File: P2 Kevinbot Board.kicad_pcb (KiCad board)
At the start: 4 copper layers, 156.5 x 85.4 mm, 45 parts, among them J1 Conn_01x03_Pin, J12 Conn_02x06_Odd_Even, J16 Conn_02x06_Odd_Even, J2 Conn_01x03_Pin, J3 USB_C_Receptacle_USB2.0_16P, J4 Conn_01x02_Pin, J5 Conn_01x02_Pin, J6 Conn_02x06_Odd_Even, J7 Conn_01x02_Pin, J8 Conn_02x06_Odd_Even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

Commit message: reset button
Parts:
- added J9: Conn_01x02_Pin, Connector_Molex:Molex_Nano-Fit_105309-xx02_1x02_P2.50mm_Vertical, F.Cu at (125.3, 58.9)
- added SW1: SW_Push, Button_Switch_SMD:SW_SPST_PTS645, F.Cu at (129.0, 96.4)
- moved JP1 4.20 mm to (120.2, 70.1)
- moved JP3 4.20 mm to (120.2, 72.7)
- moved JP2 4.20 mm to (120.2, 67.5)
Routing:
- net /P2_RESn: track 44.1 -> 88.9 mm, vias 1 -> 3
- net /Programmer/TX: track 14.2 -> 18.0 mm
- net P2_P63_RXD: track 46.2 -> 42.5 mm
- net P2_P62_TXD: track 51.2 -> 47.9 mm
- net /Programmer/RX: track 16.7 -> 19.8 mm
- net /Programmer/RESn: track 7.93 -> 9.67 mm
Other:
- board text added: "CORE RESET"

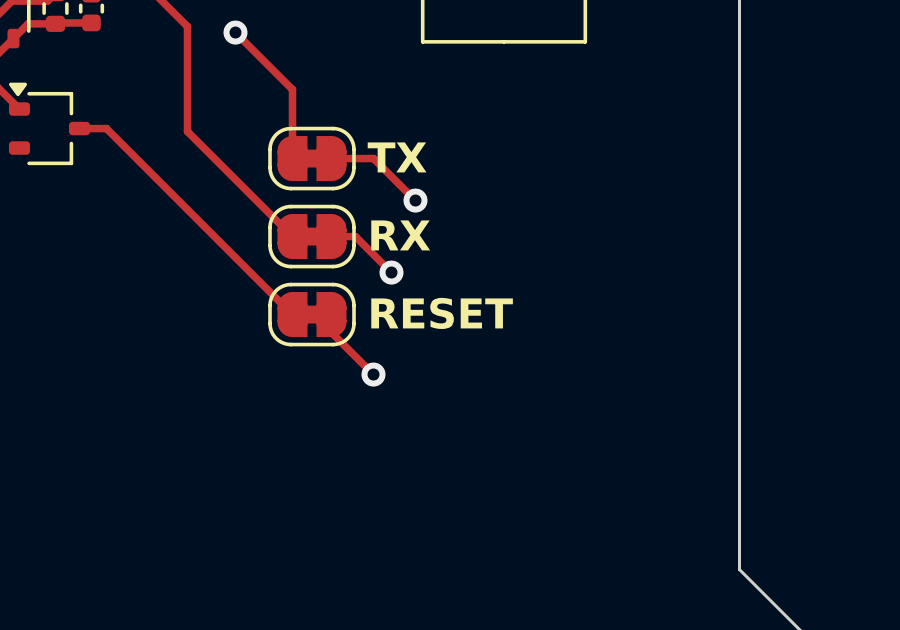
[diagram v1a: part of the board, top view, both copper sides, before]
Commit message: docs: add logo banner, pcb: reset text changes
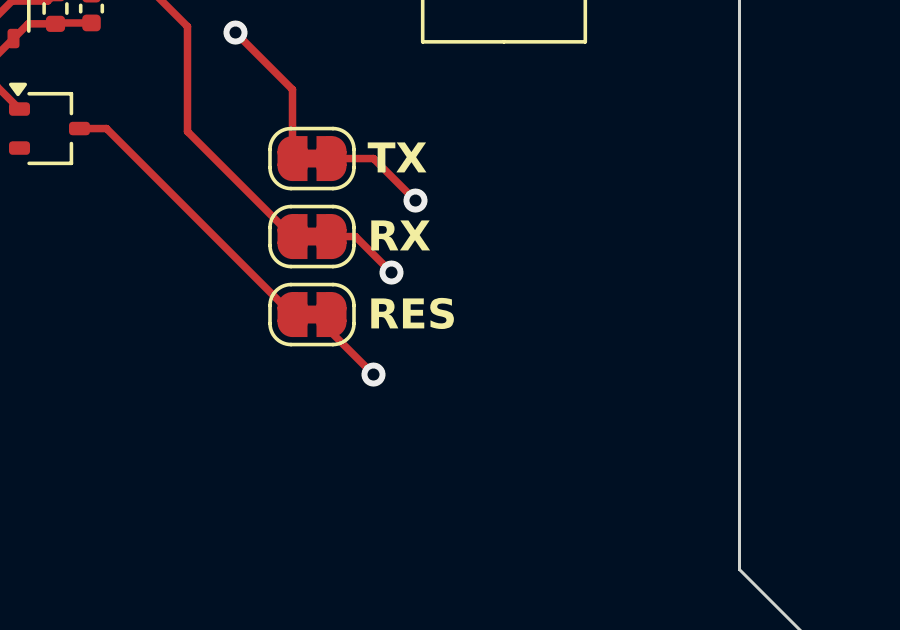
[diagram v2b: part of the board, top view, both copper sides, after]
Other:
- board text added: "RES"
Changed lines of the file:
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@@
 		)
 	)
-	(gr_text "RESET"
+	(gr_text "RES"
 		(at 122.039 72.66 0)
-		(layer "F.SilkS")
+		(layer "F.SilkS" knockout)
 		(effects
 			(font
@@
 			(justify left)
 		)
-		(render_cache "RESET" 0
+		(render_cache "RES" 0
 			(polygon
 				(pts
@@
 				)
 			)
-			(polygon
-				(pts
-					(xy 124.812621 72.090212) (xy 125.521903 72.090212) (xy 125.521903 72.250436) (xy 125.004108 72.250436)
-					(xy 125.004108 72.50054) (xy 125.48087 72.50054) (xy 125.48087 72.660764) (xy 125.004108 72.660764)
-					(xy 125.004108 72.914776) (xy 125.521903 72.914776) (xy 125.521903 73.075) (xy 124.812621 73.075)
-				)
-			)
-			(polygon
-				(pts
-					(xy 125.883382 72.250436) (xy 125.59029 72.250436) (xy 125.59029 72.090212) (xy 126.364052 72.090212)
-					(xy 126.364052 72.250436) (xy 126.074868 72.250436) (xy 126.074868 73.075) (xy 125.883382 73.075)
-				)
-			)

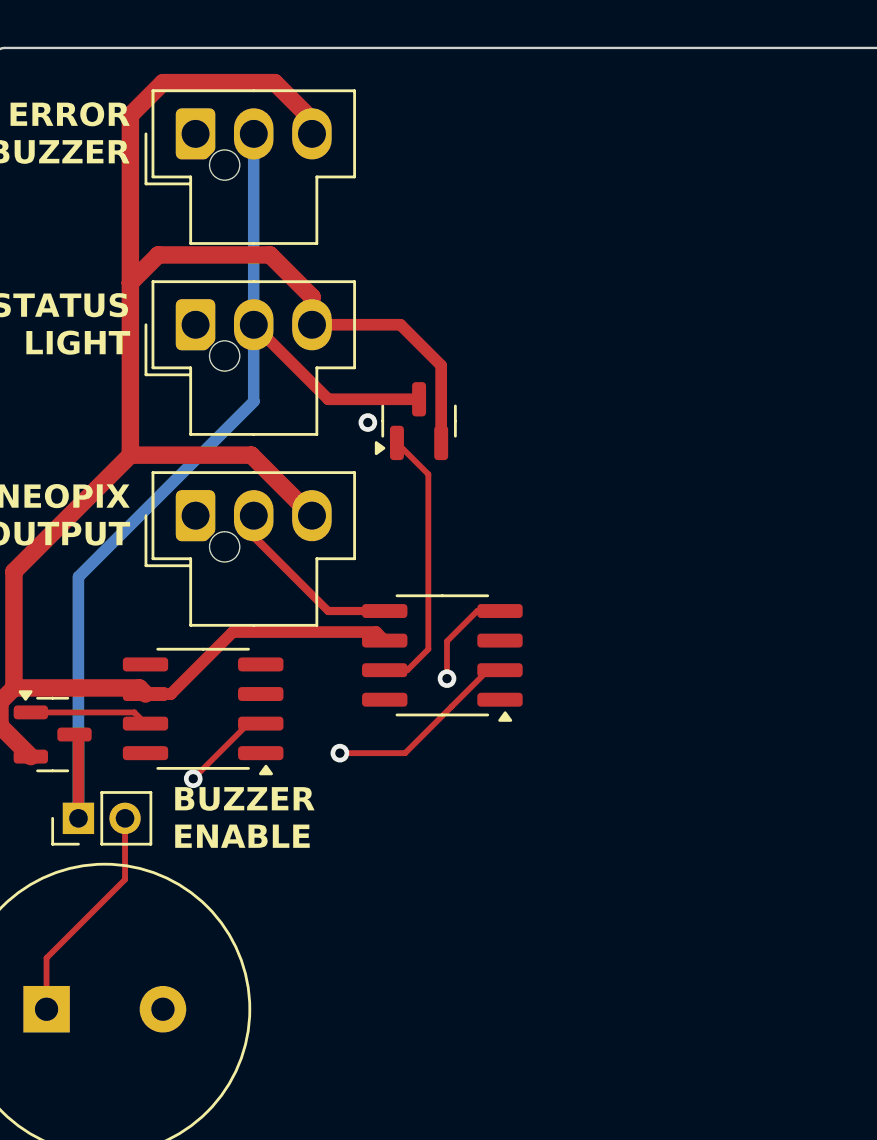
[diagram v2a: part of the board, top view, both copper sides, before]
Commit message: pcb, sch: add rs422 comm interface
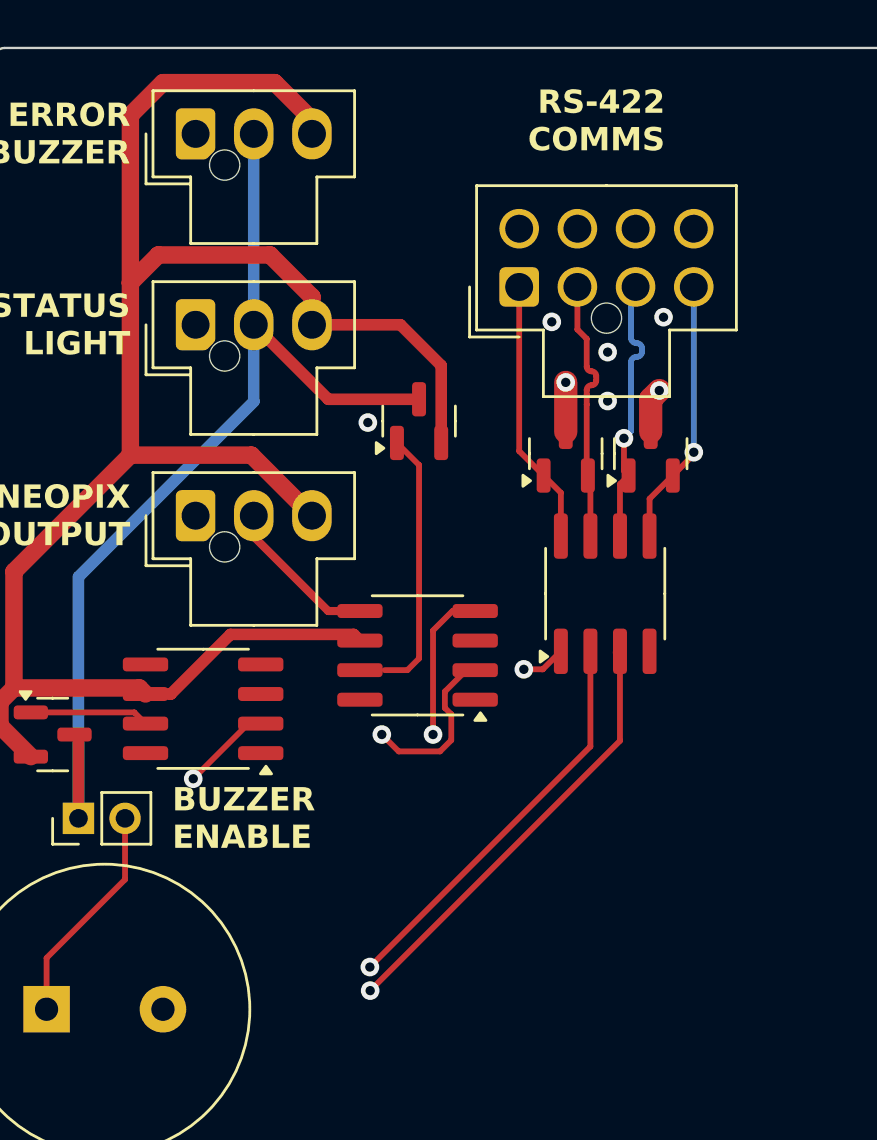
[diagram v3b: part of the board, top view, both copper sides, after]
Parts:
- added D3: D_TVS_Dual_AAC, Package_TO_SOT_SMD:SOT-23, F.Cu at (220.7, 72.6)
- added D4: D_TVS_Dual_AAC, Package_TO_SOT_SMD:SOT-23, F.Cu at (224.4, 72.6)
- added J10: Conn_02x04_Counter_Clockwise, Connector_Molex:Molex_Nano-Fit_105310-xx08_2x04_P2.50mm_Vertical, F.Cu at (218.7, 65.4)
- added U5: THVD1451D, Package_SO:SOIC-8_3.9x4.9mm_P1.27mm, F.Cu at (222.4, 78.6)
- moved U6 1.06 mm to (214.4, 81.3)
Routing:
- net P2_P35: track 0.00 -> 54.2 mm, vias 0 -> 1
- net P2_P36: track 0.00 -> 53.5 mm, vias 0 -> 1
- net P2_V32: track 0.00 -> 44.7 mm, vias 0 -> 1
- net /RS-422/D+: track 0.00 -> 11.7 mm, vias 0 -> 1
- net /RS-422/D-: track 0.00 -> 11.5 mm, vias 0 -> 1
- net /RS-422/R+: track 0.00 -> 11.4 mm
- net /RS-422/R-: track 0.00 -> 11.4 mm
- net GND: track 5.60 -> 9.66 mm, vias 2 -> 8
- net P2_P56: track 72.5 -> 74.2 mm
- net +5V: track 88.5 -> 87.3 mm
- net /LED/NPX: track 7.85 -> 6.78 mm
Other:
- board text added: "RS-422 COMMS"

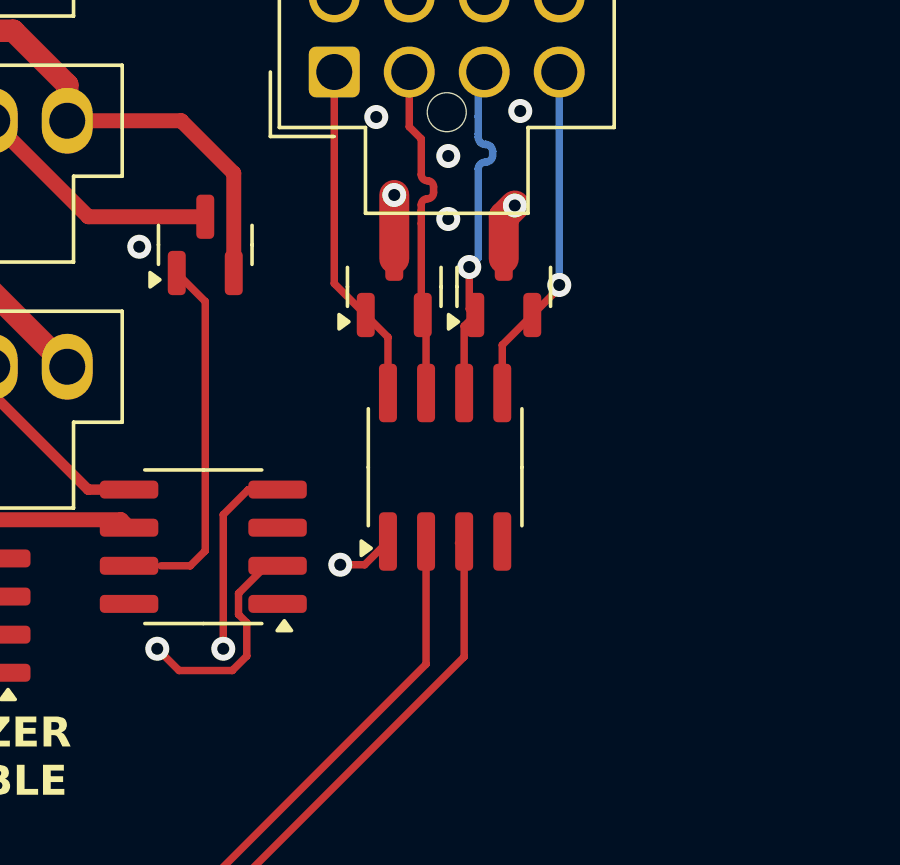
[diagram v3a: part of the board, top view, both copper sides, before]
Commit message: pcb, sch: add transciever decoupling cap, docs, wireviz: add rs422 wiring harness
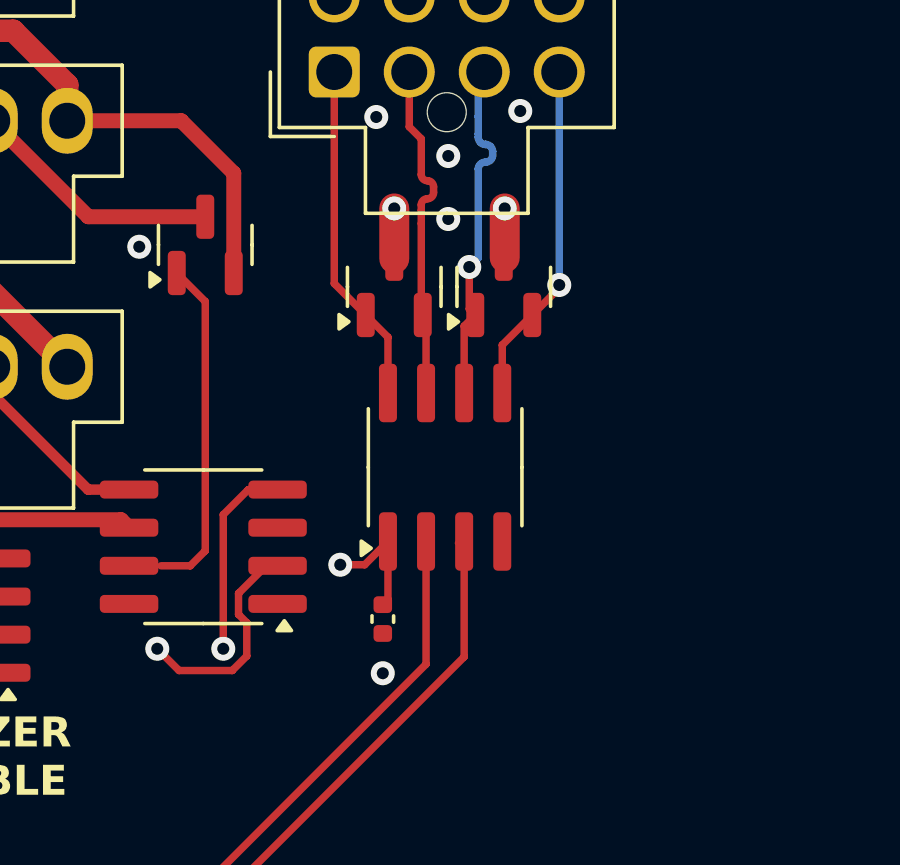
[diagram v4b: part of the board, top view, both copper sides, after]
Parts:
- added C7: 100nF, Capacitor_SMD:C_0402_1005Metric, F.Cu at (220.4, 83.7)
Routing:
- net P2_V32: track 44.7 -> 46.9 mm
- net GND: track 9.66 -> 8.93 mm, vias 8 -> 9
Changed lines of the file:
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@@
 	(footprint "Capacitor_SMD:C_0402_1005Metric"
 		(layer "F.Cu")
+		(at 220.357 83.67 90)
+		(descr "Capacitor SMD 0402 (1005 Metric), square (rectangular) end terminal, IPC-7351 nominal, (Body size source: IPC-SM-782 page 76, https://www.pcb-3d.com/wordpress/wp-content/uploads/ipc-sm-782a_amendment_1_and_2.pdf), generated with kicad-footprint-generator")
+		(tags "capacitor")
+		(property "Reference" "C7"
+			(at 0 -1.16 90)
+			(layer "F.SilkS")
+			(hide yes)
+			(effects
+				(font
+					(size 1 1)
+					(thickness 0.15)
+				)
+			)
+		)
+		(property "Value" "100nF"
+			(at 0 1.16 90)
+			(layer "F.Fab")
+			(effects
+				(font
+					(size 1 1)
+					(thickness 0.15)
+				)
+			)
+		)
+		(property "Datasheet" ""
+			(at 0 0 90)
+			(layer "F.Fab")
+			(hide yes)
+			(effects
+				(font
+					(size 1.27 1.27)
+					(thickness 0.15)
+				)
+			)
+		)
+		(property "Description" "Unpolarized capacitor"
+			(at 0 0 90)
+			(layer "F.Fab")
+			(hide yes)
+			(effects
+				(font
+					(size 1.27 1.27)
+					(thickness 0.15)
+				)
+			)
+		)
+		(property ki_fp_filters "C_*")
+		(sheetname "/RS-422/")
+		(sheetfile "rs422.kicad_sch")
+		(attr smd)
+		(fp_line
+			(start -0.107836 -0.36)
+			(end 0.107836 -0.36)
+			(stroke
+				(width 0.12)
+				(type solid)
+			)
+			(layer "F.SilkS")
+		)
+		(fp_line
+			(start -0.107836 0.36)
+			(end 0.107836 0.36)
+			(stroke
+				(width 0.12)
+				(type solid)
+			)
+			(layer "F.SilkS")
+		)
+		(fp_line
+			(start 0.91 -0.46)
+			(end 0.91 0.46)
+			(stroke
+				(width 0.05)
+				(type solid)
+			)
+			(layer "F.CrtYd")
+		)
+		(fp_line
+			(start -0.91 -0.46)
+			(end 0.91 -0.46)
+			(stroke
+				(width 0.05)
+				(type solid)
+			)
+			(layer "F.CrtYd")
+		)
+		(fp_line
+			(start 0.91 0.46)
+			(end -0.91 0.46)
+			(stroke
+				(width 0.05)
+				(type solid)
+			)
+			(layer "F.CrtYd")
+		)
+		(fp_line
+			(start -0.91 0.46)
+			(end -0.91 -0.46)
+			(stroke
+				(width 0.05)
+				(type solid)
+			)
+			(layer "F.CrtYd")
+		)
+		(fp_line
+			(start 0.5 -0.25)
+			(end 0.5 0.25)
+			(stroke
+				(width 0.1)
+				(type solid)
+			)
+			(layer "F.Fab")
+		)
+		(fp_line
+			(start -0.5 -0.25)
+			(end 0.5 -0.25)
+			(stroke
+				(width 0.1)
+				(type solid)
+			)
+			(layer "F.Fab")
+		)
+		(fp_line
+			(start 0.5 0.25)
+			(end -0.5 0.25)
+			(stroke
+				(width 0.1)
+				(type solid)
+			)
+			(layer "F.Fab")
+		)
+		(fp_line
+			(start -0.5 0.25)
+			(end -0.5 -0.25)
+			(stroke
+				(width 0.1)
+				(type solid)
+			)
+			(layer "F.Fab")
+		)
+		(fp_text user "${REFERENCE}"
+			(at 0 0 90)
+			(layer "F.Fab")
+			(effects
+				(font
+					(size 0.25 0.25)
+					(thickness 0.04)
+				)
+			)
+		)
+		(pad "1" smd roundrect
+			(at -0.48 0 90)
+			(size 0.56 0.62)
+			(layers "F.Cu" "F.Mask" "F.Paste")
+			(roundrect_rratio 0.25)
+			(net 4 "GND")
+			(pintype "passive")
+		)
+		(pad "2" smd roundrect
+			(at 0.48 0 90)
+			(size 0.56 0.62)
+			(layers "F.Cu" "F.Mask" "F.Paste")
+			(roundrect_rratio 0.25)
+			(net 73 "P2_V32")
+			(pintype "passive")
+		)
+		(embedded_fonts no)
+		(model "${KICAD9_3DMODEL_DIR}/Capacitor_SMD.3dshapes/C_0402_1005Metric.wrl"
+			(offset
+				(xyz 0 0 0)
+			)
+			(scale
+				(xyz 1 1 1)
+			)
+			(rotate
+				(xyz 0 0 0)
+			)
+		)
+	)
+	(footprint "Capacitor_SMD:C_0402_1005Metric"
+		(layer "F.Cu")
 		(at 108.039 65.06)
 		(descr "Capacitor SMD 0402 (1005 Metric), square (rectangular) end terminal, IPC_7351 nominal, (Body size source: IPC-SM-782 page 76, https://www.pcb-3d.com/wordpress/wp-content/uploads/ipc-sm-782a_amendment_1_and_2.pdf), generated with kicad-footprint-generator")
@@
 	)
 	(segment
-		(start 224.389 70.252907)
-		(end 224.756907 69.885)
+		(start 220.739 71.66)
+		(end 220.739 69.982)
 		(width 1)
 		(layer "F.Cu")
@@
 	)
 	(segment
-		(start 224.389 71.66)
-		(end 224.389 70.252907)
-		(width 1)
-		(layer "F.Cu")
-		(net 4)
-	)
-	(segment
-		(start 220.739 71.66)
-		(end 220.739 69.535)
-		(width 1)
-		(layer "F.Cu")
-		(net 4)
-	)
-	(segment
 		(start 93.774029 63.885)
 		(end 93.199029 63.31)
@@
 	)
 	(segment
+		(start 224.421 69.982)
+		(end 224.421 71.628)
+		(width 1)
+		(layer "F.Cu")
+		(net 4)
+	)
+	(segment
 		(start 143.241264 101.43)
 		(end 144.511264 100.16)
@@
 	)
 	(via
-		(at 220.739 69.535)
+		(at 220.739 69.982)
 		(size 0.8)
 		(drill 0.4)
@@
 	)
 	(via
-		(at 224.756907 69.885)
+		(at 224.421 69.982)
 		(size 0.8)
 		(drill 0.4)
@@
 	)
 	(via
+		(at 220.357 85.476)
+		(size 0.8)
+		(drill 0.4)
+		(layers "F.Cu" "B.Cu")
+		(free yes)
+		(net 4)
+	)
+	(via
 		(at 97.539 68.81)
 		(size 0.8)
@@
 	)
 	(segment
+		(start 220.529 83.018)
+		(end 220.529 81.085)
+		(width 0.25)
+		(layer "F.Cu")
+		(net 73)
+	)
+	(segment
 		(start 220.529 81.085)
 		(end 219.754 81.86)
 		(width 0.25)
 		(layer "F.Cu")
+		(net 73)
+	)
+	(segment
+		(start 220.357 83.19)
+		(end 220.529 83.018)
+		(width 0.25)
+		(layer "F.Cu")

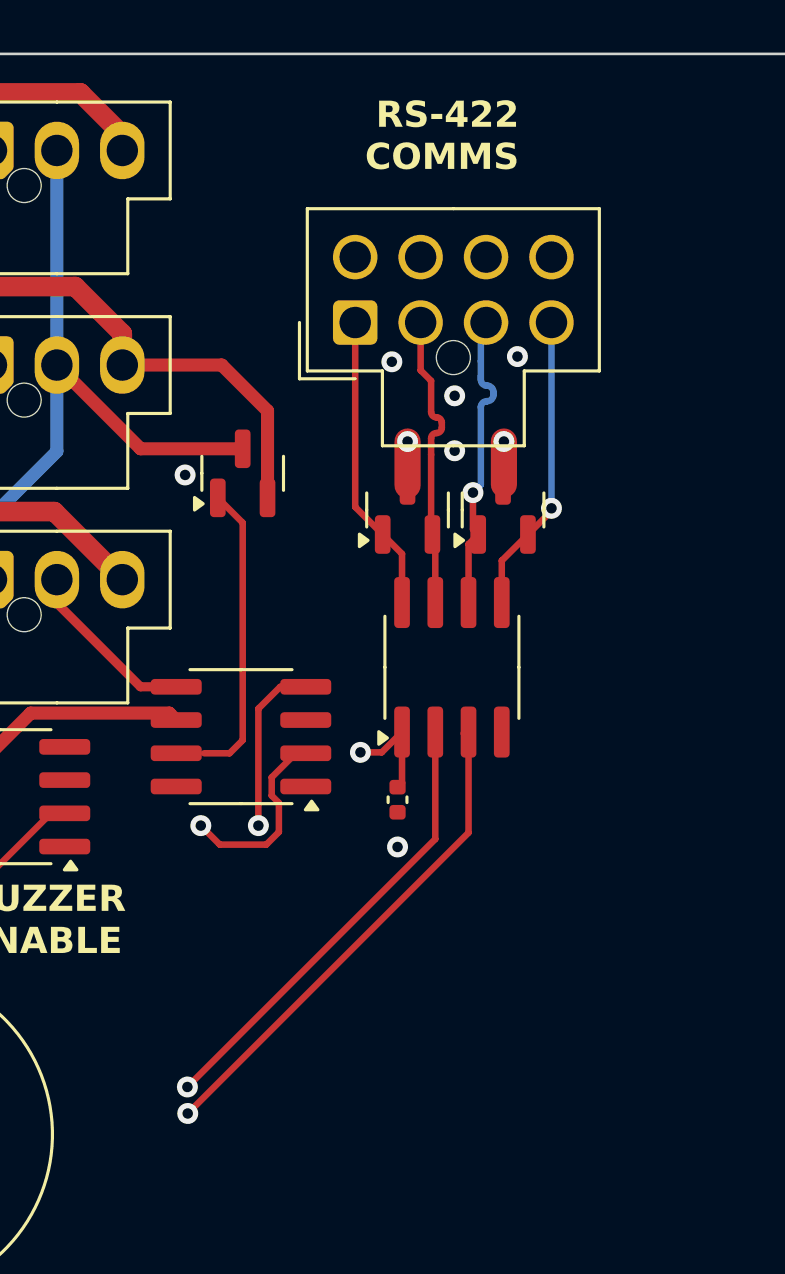
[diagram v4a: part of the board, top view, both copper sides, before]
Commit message: pcb: relocate rs422
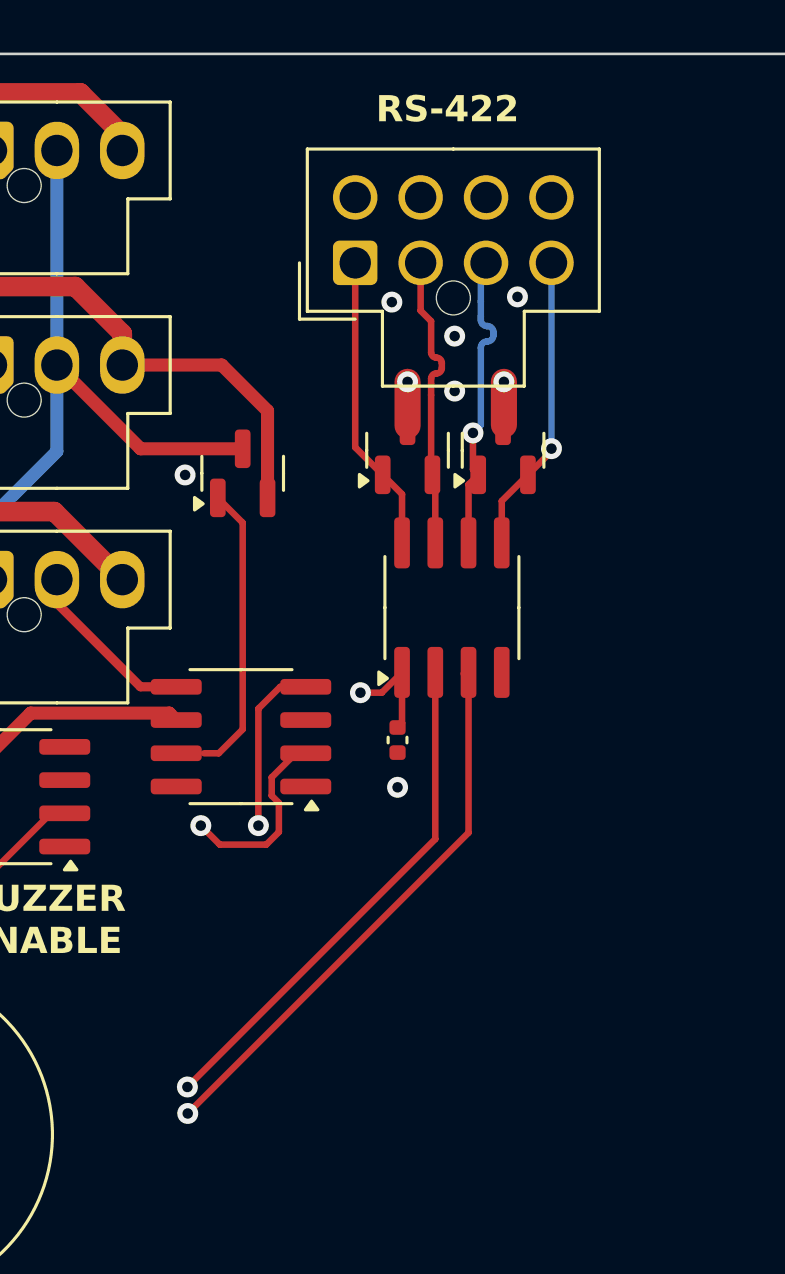
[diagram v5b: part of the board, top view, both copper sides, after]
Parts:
- moved C7 2.28 mm to (220.4, 81.4)
- moved D3 2.28 mm to (220.7, 70.3)
- moved D4 2.28 mm to (224.4, 70.3)
- moved J10 2.28 mm to (218.7, 63.2)
- moved U5 2.28 mm to (222.4, 76.3)
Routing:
- net P2_P36: track 53.5 -> 55.8 mm
- net P2_P35: track 54.2 -> 56.5 mm
- net P2_V32: track 46.9 -> 48.5 mm
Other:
- board text added: "RS-422"
- board text removed: "RS-422 COMMS"

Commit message: pcb, sch: mounting holes
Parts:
- added H1: MountingHole_Pad, MountingHole:MountingHole_3.2mm_M3_Pad, F.Cu at (92.1, 79.1)
- added H2: MountingHole_Pad, MountingHole:MountingHole_3.2mm_M3_Pad, F.Cu at (236.1, 61.1)
- added H3: MountingHole_Pad, MountingHole:MountingHole_3.2mm_M3_Pad, F.Cu at (92.1, 133.1)
- added H4: MountingHole_Pad, MountingHole:MountingHole_3.2mm_M3_Pad, F.Cu at (236.1, 133.1)
